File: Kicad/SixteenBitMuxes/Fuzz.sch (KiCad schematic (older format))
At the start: 11 parts, among them J2 POT B10K JST XH, J3 POT B5K JST XH, J4 VOL POT A100K JST XH

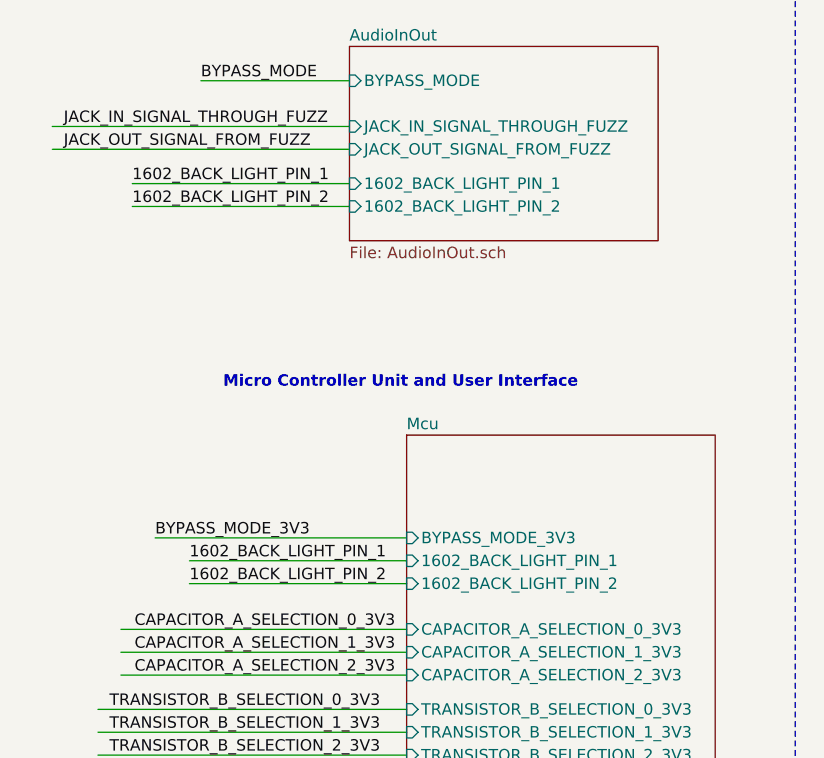
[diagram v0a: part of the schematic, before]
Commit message: LCD backlight and backlight removed from circuit/pcb.
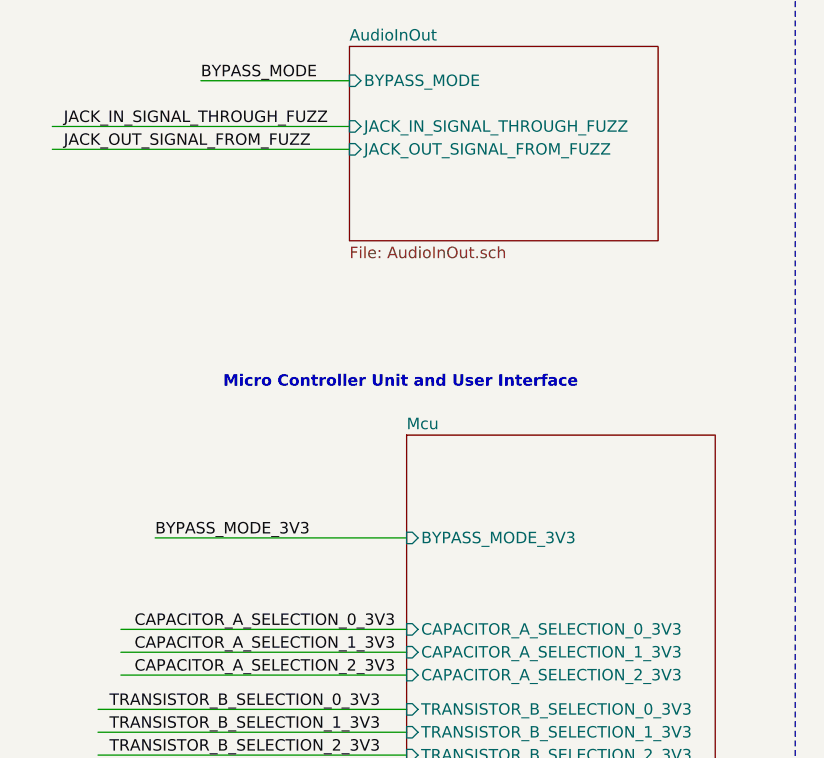
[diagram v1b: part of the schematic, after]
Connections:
- net labels removed: 1602_BACK_LIGHT_PIN_1, 1602_BACK_LIGHT_PIN_2
- wire segments 98 -> 94
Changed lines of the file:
@@
 F3 "JACK_IN_SIGNAL_THROUGH_FUZZ" I L 1950 3750 50
 F4 "JACK_OUT_SIGNAL_FROM_FUZZ" I L 1950 3850 50
-F5 "1602_BACK_LIGHT_PIN_1" I L 1950 4000 50
-F6 "1602_BACK_LIGHT_PIN_2" I L 1950 4100 50
 $EndSheet
 Text Label 6100 5400 0    50   ~ 0
@@
 Text Label 1100 5550 0    50   ~ 0
 BYPASS_MODE_3V3
-Text Label 1250 5650 0    50   ~ 0
-1602_BACK_LIGHT_PIN_1
-Text Label 1250 5750 0    50   ~ 0
-1602_BACK_LIGHT_PIN_2
-Wire Wire Line
-	1250 5650 2200 5650
-Wire Wire Line
-	2200 5750 1250 5750
-Text Label 1000 4000 0    50   ~ 0
-1602_BACK_LIGHT_PIN_1
-Text Label 1000 4100 0    50   ~ 0
-1602_BACK_LIGHT_PIN_2
-Wire Wire Line
-	1000 4000 1950 4000
-Wire Wire Line
-	1950 4100 1000 4100
 Wire Wire Line
 	650  3750 1950 3750
@@
 F0 "Mcu" 50
 F1 "Mcu.sch" 50
-F2 "1602_BACK_LIGHT_PIN_1" I L 2200 5650 50
-F3 "1602_BACK_LIGHT_PIN_2" I L 2200 5750 50
-F4 "BYPASS_MODE_3V3" I L 2200 5550 50
-F5 "TRANSISTOR_B_SELECTION_0_3V3" I L 2200 6300 50
-F6 "TRANSISTOR_B_SELECTION_1_3V3" I L 2200 6400 50
-F7 "TRANSISTOR_B_SELECTION_2_3V3" I L 2200 6500 50
-F8 "TRANSISTOR_B_SELECTION_3_3V3" I L 2200 6600 50
-F9 "CAPACITOR_A_SELECTION_0_3V3" I L 2200 5950 50
-F10 "CAPACITOR_A_SELECTION_1_3V3" I L 2200 6050 50
-F11 "CAPACITOR_A_SELECTION_2_3V3" I L 2200 6150 50
-F12 "TRANSISTOR_C_SELECTION_0_3V3" I L 2200 6750 50
-F13 "TRANSISTOR_C_SELECTION_1_3V3" I L 2200 6850 50
-F14 "TRANSISTOR_C_SELECTION_2_3V3" I L 2200 6950 50
-F15 "TRANSISTOR_C_SELECTION_3_3V3" I L 2200 7050 50
-F16 "CAPACITOR_D_SELECTION_0_3V3" I L 2200 7200 50
-F17 "CAPACITOR_D_SELECTION_1_3V3" I L 2200 7300 50
-F18 "CAPACITOR_D_SELECTION_2_3V3" I L 2200 7400 50
+F2 "BYPASS_MODE_3V3" I L 2200 5550 50
+F3 "TRANSISTOR_B_SELECTION_0_3V3" I L 2200 6300 50
+F4 "TRANSISTOR_B_SELECTION_1_3V3" I L 2200 6400 50
+F5 "TRANSISTOR_B_SELECTION_2_3V3" I L 2200 6500 50
+F6 "TRANSISTOR_B_SELECTION_3_3V3" I L 2200 6600 50
+F7 "CAPACITOR_A_SELECTION_0_3V3" I L 2200 5950 50
+F8 "CAPACITOR_A_SELECTION_1_3V3" I L 2200 6050 50
+F9 "CAPACITOR_A_SELECTION_2_3V3" I L 2200 6150 50
+F10 "TRANSISTOR_C_SELECTION_0_3V3" I L 2200 6750 50
+F11 "TRANSISTOR_C_SELECTION_1_3V3" I L 2200 6850 50
+F12 "TRANSISTOR_C_SELECTION_2_3V3" I L 2200 6950 50
+F13 "TRANSISTOR_C_SELECTION_3_3V3" I L 2200 7050 50
+F14 "CAPACITOR_D_SELECTION_0_3V3" I L 2200 7200 50
+F15 "CAPACITOR_D_SELECTION_1_3V3" I L 2200 7300 50
+F16 "CAPACITOR_D_SELECTION_2_3V3" I L 2200 7400 50
 $EndSheet
 $EndSCHEMATC

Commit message: EEprom + PCB changes
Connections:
- wire segments 94 -> 95
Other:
- moved on the sheet: C1, J2, J3, J4, R1, R2, R3

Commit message: PCB mostly
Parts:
- removed J2: POT B10K JST XH, Connector_JST:JST_XH_B2B-XH-A_1x02_P2.50mm_Vertical, symbol Connector:Conn_01x02_Male
- removed J3: POT B5K JST XH, Connector_JST:JST_XH_B2B-XH-A_1x02_P2.50mm_Vertical, symbol Connector:Conn_01x02_Male
- added J2: TONE_POTS, Connector_JST:JST_XH_B4B-XH-A_1x04_P2.50mm_Vertical, symbol Connector:Conn_01x04_Male
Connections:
- net labels added: B10K, B5K
- wire segments 95 -> 98
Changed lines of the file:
@@
 $EndComp
-$Comp
-L Connector:Conn_01x02_Male J2
-U 1 1 5EC4B1FB
-P 5650 2750
-F 0 "J2" H 5758 2931 50  0000 C CNN
-F 1 "POT B10K JST XH" H 5758 2840 50  0000 C CNN
-F 2 "Connector_JST:JST_XH_B2B-XH-A_1x02_P2.50mm_Vertical" H 5650 2750 50  0001 C CNN
-F 3 "~" H 5650 2750 50  0001 C CNN
-	1    5650 2750
-	1    0    0    -1
-$EndComp
-$Comp
-L Connector:Conn_01x02_Male J3
-U 1 1 5EC4BC76
-P 6400 2750
-F 0 "J3" H 6508 2931 50  0000 C CNN
-F 1 "POT B5K JST XH" H 6508 2840 50  0000 C CNN
-F 2 "Connector_JST:JST_XH_B2B-XH-A_1x02_P2.50mm_Vertical" H 6400 2750 50  0001 C CNN
-F 3 "~" H 6400 2750 50  0001 C CNN
-	1    6400 2750
-	1    0    0    -1
-$EndComp
-Wire Wire Line
-	5850 2850 5850 2950
 $Comp
 L Device:CP1 C1
@@
 Wire Wire Line
 	5450 1200 5450 1150
-Wire Wire Line
-	6600 2450 6600 2750
 Wire Wire Line
 	5850 2450 5850 2750
@@
 	900  4550 2200 4550
 $Comp
-L power:GNDA #PWR03
-U 1 1 5EA13AD0
-P 5850 2950
-F 0 "#PWR03" H 5850 2700 50  0001 C CNN
-F 1 "GNDA" H 5855 2777 50  0000 C CNN
-F 2 "" H 5850 2950 50  0001 C CNN
-F 3 "" H 5850 2950 50  0001 C CNN
-	1    5850 2950
-	1    0    0    -1
-$EndComp
-$Comp
 L power:GNDA #PWR04
 U 1 1 5EA14305
@@
 F 3 "" H 10600 2600 50  0001 C CNN
 	1    10600 2600
-	1    0    0    -1
-$EndComp
-$Comp
-L power:GNDA #PWR02
-U 1 1 5EA15848
-P 5450 2150
-F 0 "#PWR02" H 5450 1900 50  0001 C CNN
-F 1 "GNDA" H 5455 1977 50  0000 C CNN
-F 2 "" H 5450 2150 50  0001 C CNN
-F 3 "" H 5450 2150 50  0001 C CNN
-	1    5450 2150
 	1    0    0    -1
 $EndComp
@@
 Wire Wire Line
 	5450 1500 5450 2050
-Wire Wire Line
-	6600 2850 6600 3050
+$Comp
+L Connector:Conn_01x04_Male J2
+U 1 1 5ED44307
+P 4950 2850
+F 0 "J2" H 5058 3131 50  0000 C CNN
+F 1 "TONE_POTS" H 5058 3040 50  0000 C CNN
+F 2 "Connector_JST:JST_XH_B4B-XH-A_1x04_P2.50mm_Vertical" H 4950 2850 50  0001 C CNN
+F 3 "~" H 4950 2850 50  0001 C CNN
+	1    4950 2850
+	1    0    0    -1
+$EndComp
+Wire Wire Line
+	5150 2750 5850 2750
+Wire Wire Line
+	5850 2850 5150 2850
+$Comp
+L power:GNDA #PWR03
+U 1 1 5EA13AD0
+P 5850 3250
+F 0 "#PWR03" H 5850 3000 50  0001 C CNN
+F 1 "GNDA" H 5855 3077 50  0000 C CNN
+F 2 "" H 5850 3250 50  0001 C CNN
+F 3 "" H 5850 3250 50  0001 C CNN
+	1    5850 3250
+	1    0    0    -1
+$EndComp
+Wire Wire Line
+	5850 2850 5850 3250
+Wire Wire Line
+	5150 3050 6600 3050
+Wire Wire Line
+	6600 2450 6600 2950
+Wire Wire Line
+	5150 2950 6600 2950
+Text Label 5350 2750 0    50   ~ 0
+B10K
+$Comp
+L power:GNDA #PWR02
+U 1 1 5EA15848
+P 5450 2150
+F 0 "#PWR02" H 5450 1900 50  0001 C CNN
+F 1 "GNDA" H 5455 1977 50  0000 C CNN
+F 2 "" H 5450 2150 50  0001 C CNN
+F 3 "" H 5450 2150 50  0001 C CNN
+	1    5450 2150
+	1    0    0    -1
+$EndComp
+Text Label 5350 2950 0    50   ~ 0
+B5K
 $EndSCHEMATC

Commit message: Improvements according video youtube
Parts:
- removed H1, H2, H3, H4: MountingHole, MountingHole:MountingHole_3.2mm_M3, symbol Mechanical:MountingHole
- added H1, H2, H3, H4: MountingHole_Pad, MountingHole:MountingHole_3mm_Pad_Via, symbol Mechanical:MountingHole_Pad
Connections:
- net labels added: +9V_SAFE, GND
- net labels removed: +9V
- wire segments 98 -> 110
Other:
- moved on the sheet: J4
